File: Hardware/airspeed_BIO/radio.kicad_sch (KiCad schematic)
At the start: 9 parts, among them J3 RF, SW2 434123025826, U5 2607011111000

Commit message: set Ilimit and set footprint
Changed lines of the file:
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@@
 	)
 	(label "RST"
-		(at 128.27 99.06 180)
+		(at 129.54 99.06 180)
 		(effects
 			(font

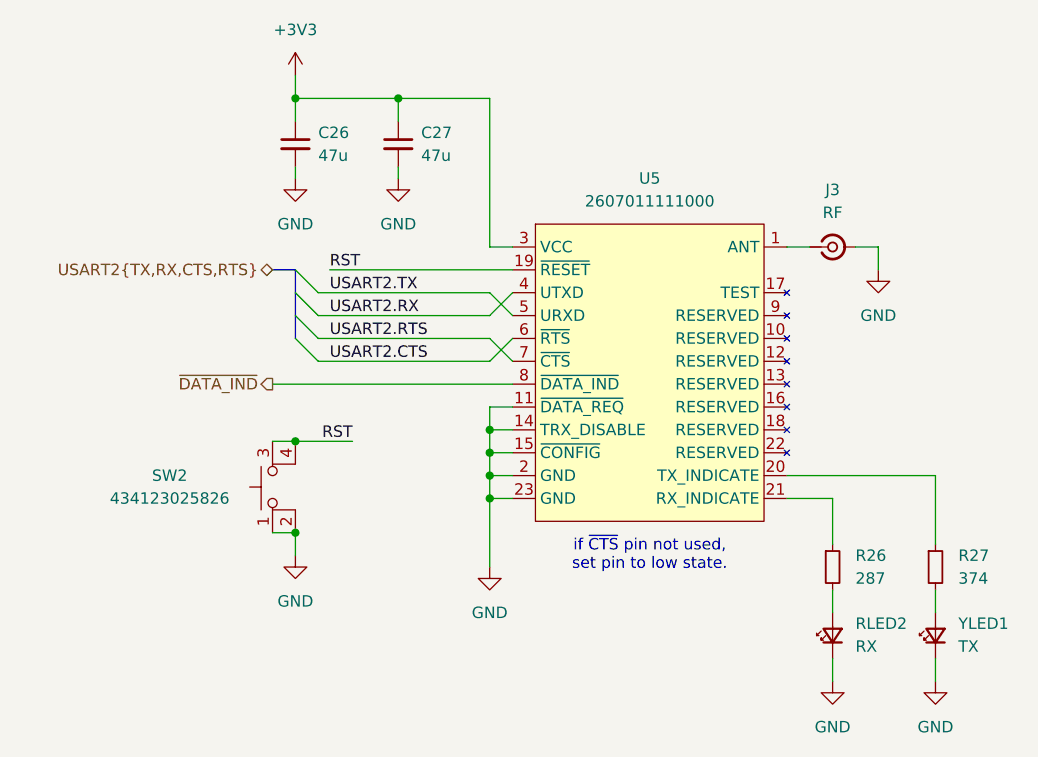
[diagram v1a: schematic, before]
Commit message: layout and fix Schematic
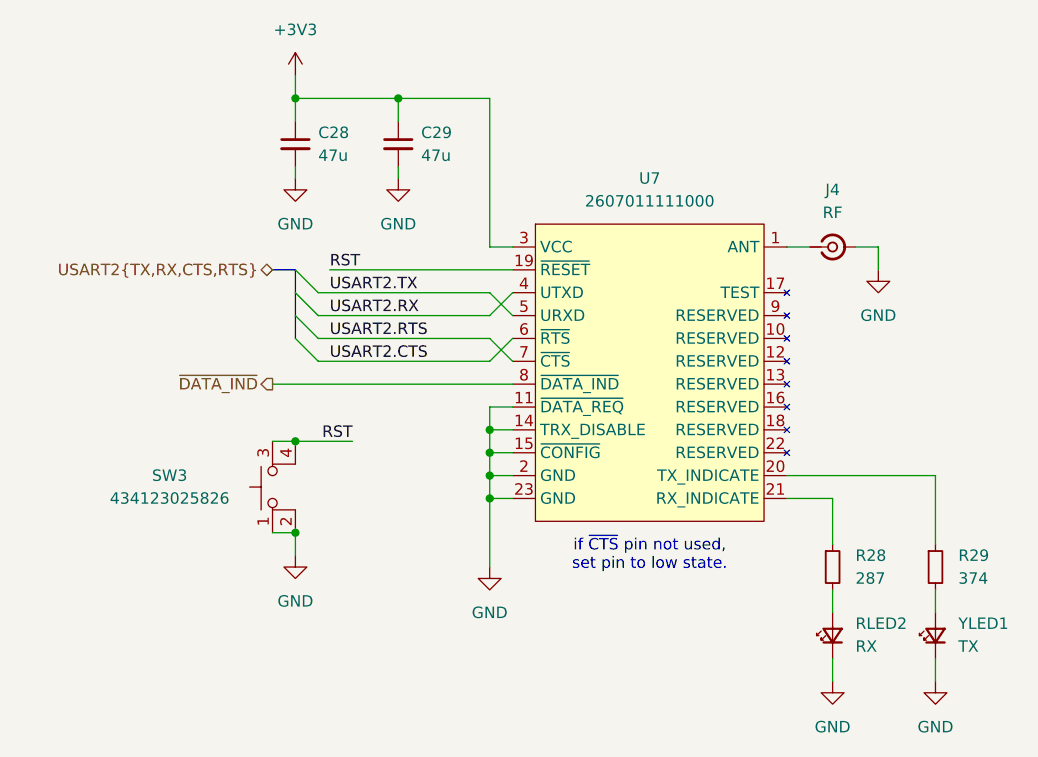
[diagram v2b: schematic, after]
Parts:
- renumbered C26 to C28, C27 to C29, J3 to J4, R26 to R28, R27 to R29, SW2 to SW3, U5 to U7
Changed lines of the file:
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@@
 		(dnp no)
 		(fields_autoplaced yes)
-		(property "Reference" "#PWR042"
+		(property "Reference" "#PWR051"
 			(at 194.31 132.08 0)
 			(effects
@@
 			(project "airspeed_BIO"
 				(path "/6ddcf4fe-9e51-4114-8222-5fc3f810c12a/bc5e8fae-35c8-4595-bef2-c7c6a3d6b7bb"
-					(reference "#PWR042")
+					(reference "#PWR051")
 					(unit 1)
 				)
@@
 		(dnp no)
 		(fields_autoplaced yes)
-		(property "Reference" "R27"
+		(property "Reference" "R29"
 			(at 196.85 111.7599 0)
 			(effects
@@
 			(project "airspeed_BIO"
 				(path "/6ddcf4fe-9e51-4114-8222-5fc3f810c12a/bc5e8fae-35c8-4595-bef2-c7c6a3d6b7bb"
-					(reference "R27")
+					(reference "R29")
 					(unit 1)
 				)
@@
 		(dnp no)
 		(fields_autoplaced yes)
-		(property "Reference" "C26"
+		(property "Reference" "C28"
 			(at 125.73 64.7762 0)
 			(effects
@@
 			(project "airspeed_BIO"
 				(path "/6ddcf4fe-9e51-4114-8222-5fc3f810c12a/bc5e8fae-35c8-4595-bef2-c7c6a3d6b7bb"
-					(reference "C26")
+					(reference "C28")
 					(unit 1)
 				)
@@
 		(on_board yes)
 		(dnp no)
-		(property "Reference" "SW2"
+		(property "Reference" "SW3"
 			(at 109.22 102.87 90)
 			(effects
@@
 			(project "airspeed_BIO"
 				(path "/6ddcf4fe-9e51-4114-8222-5fc3f810c12a/bc5e8fae-35c8-4595-bef2-c7c6a3d6b7bb"
-					(reference "SW2")
+					(reference "SW3")
 					(unit 1)
 				)
@@
 		(dnp no)
 		(fields_autoplaced yes)
-		(property "Reference" "R26"
+		(property "Reference" "R28"
 			(at 185.42 111.7599 0)
 			(effects
@@
 			(project "airspeed_BIO"
 				(path "/6ddcf4fe-9e51-4114-8222-5fc3f810c12a/bc5e8fae-35c8-4595-bef2-c7c6a3d6b7bb"
-					(reference "R26")
+					(reference "R28")
 					(unit 1)
 				)
@@
 		(dnp no)
 		(fields_autoplaced yes)
-		(property "Reference" "#PWR040"
+		(property "Reference" "#PWR049"
 			(at 182.88 132.08 0)
 			(effects
@@
 			(project "airspeed_BIO"
 				(path "/6ddcf4fe-9e51-4114-8222-5fc3f810c12a/bc5e8fae-35c8-4595-bef2-c7c6a3d6b7bb"
-					(reference "#PWR040")
+					(reference "#PWR049")
 					(unit 1)
 				)
@@
 		(dnp no)
 		(fields_autoplaced yes)
-		(property "Reference" "U5"
+		(property "Reference" "U7"
 			(at 162.56 69.85 0)
 			(effects
@@
 			(project "airspeed_BIO"
 				(path "/6ddcf4fe-9e51-4114-8222-5fc3f810c12a/bc5e8fae-35c8-4595-bef2-c7c6a3d6b7bb"
-					(reference "U5")
+					(reference "U7")
 					(unit 1)
 				)
@@
 		(dnp no)
 		(fields_autoplaced yes)
-		(property "Reference" "C27"
+		(property "Reference" "C29"
 			(at 137.16 64.7762 0)
 			(effects
@@
 			(project "airspeed_BIO"
 				(path "/6ddcf4fe-9e51-4114-8222-5fc3f810c12a/bc5e8fae-35c8-4595-bef2-c7c6a3d6b7bb"
-					(reference "C27")
+					(reference "C29")
 					(unit 1)
 				)
@@
 		(dnp no)
 		(fields_autoplaced yes)
-		(property "Reference" "#PWR038"
+		(property "Reference" "#PWR047"
 			(at 134.62 76.2 0)
 			(effects
@@
 			(project "airspeed_BIO"
 				(path "/6ddcf4fe-9e51-4114-8222-5fc3f810c12a/bc5e8fae-35c8-4595-bef2-c7c6a3d6b7bb"
-					(reference "#PWR038")
+					(reference "#PWR047")
 					(unit 1)
 				)
@@
 		(dnp no)
 		(fields_autoplaced yes)
-		(property "Reference" "#PWR035"
+		(property "Reference" "#PWR044"
 			(at 123.19 62.23 0)
 			(effects
@@
 			(project ""
 				(path "/6ddcf4fe-9e51-4114-8222-5fc3f810c12a/bc5e8fae-35c8-4595-bef2-c7c6a3d6b7bb"
-					(reference "#PWR035")
+					(reference "#PWR044")
 					(unit 1)
 				)
@@
 		(dnp no)
 		(fields_autoplaced yes)
-		(property "Reference" "#PWR036"
+		(property "Reference" "#PWR045"
 			(at 123.19 76.2 0)
 			(effects
@@
 			(project "airspeed_BIO"
 				(path "/6ddcf4fe-9e51-4114-8222-5fc3f810c12a/bc5e8fae-35c8-4595-bef2-c7c6a3d6b7bb"
-					(reference "#PWR036")
+					(reference "#PWR045")
 					(unit 1)
 				)
@@
 		(on_board yes)
 		(dnp no)
-		(property "Reference" "J3"
+		(property "Reference" "J4"
 			(at 182.88 71.12 0)
 			(effects
@@
 			(project "airspeed_BIO"
 				(path "/6ddcf4fe-9e51-4114-8222-5fc3f810c12a/bc5e8fae-35c8-4595-bef2-c7c6a3d6b7bb"
-					(reference "J3")
+					(reference "J4")
 					(unit 1)
 				)
@@
 		(dnp no)
 		(fields_autoplaced yes)
-		(property "Reference" "#PWR037"
+		(property "Reference" "#PWR046"
 			(at 123.19 118.11 0)
 			(effects
@@
 			(project "airspeed_BIO"
 				(path "/6ddcf4fe-9e51-4114-8222-5fc3f810c12a/bc5e8fae-35c8-4595-bef2-c7c6a3d6b7bb"
-					(reference "#PWR037")
+					(reference "#PWR046")
 					(unit 1)
 				)
@@
 		(dnp no)
 		(fields_autoplaced yes)
-		(property "Reference" "#PWR041"
+		(property "Reference" "#PWR050"
 			(at 187.96 86.36 0)
 			(effects
@@
 			(project "airspeed_BIO"
 				(path "/6ddcf4fe-9e51-4114-8222-5fc3f810c12a/bc5e8fae-35c8-4595-bef2-c7c6a3d6b7bb"
-					(reference "#PWR041")
+					(reference "#PWR050")
 					(unit 1)
 				)
@@
 		(dnp no)
 		(fields_autoplaced yes)
-		(property "Reference" "#PWR039"
+		(property "Reference" "#PWR048"
 			(at 144.78 119.38 0)
 			(effects
@@
 			(project ""
 				(path "/6ddcf4fe-9e51-4114-8222-5fc3f810c12a/bc5e8fae-35c8-4595-bef2-c7c6a3d6b7bb"
-					(reference "#PWR039")
-					(unit 1)
-				)
+					(reference "#PWR048")
+					(unit 1)
+				)

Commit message: layoyt end
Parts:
- renumbered C28 to C27, C29 to C28
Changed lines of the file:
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@@
 		(dnp no)
 		(fields_autoplaced yes)
-		(property "Reference" "C28"
+		(property "Reference" "C27"
 			(at 125.73 64.7762 0)
 			(effects
@@
 			(project "airspeed_BIO"
 				(path "/6ddcf4fe-9e51-4114-8222-5fc3f810c12a/bc5e8fae-35c8-4595-bef2-c7c6a3d6b7bb"
-					(reference "C28")
+					(reference "C27")
 					(unit 1)
 				)
@@
 		(dnp no)
 		(fields_autoplaced yes)
-		(property "Reference" "C29"
+		(property "Reference" "C28"
 			(at 137.16 64.7762 0)
 			(effects
@@
 			(project "airspeed_BIO"
 				(path "/6ddcf4fe-9e51-4114-8222-5fc3f810c12a/bc5e8fae-35c8-4595-bef2-c7c6a3d6b7bb"
-					(reference "C29")
-					(unit 1)
-				)
+					(reference "C28")
+					(unit 1)
+				)
